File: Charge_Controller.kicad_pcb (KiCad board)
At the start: 2 copper layers, 134.6 x 76.2 mm, 156 parts, among them J1 SOLAR, J10 Conn_01x01_Female, J11 Conn_01x01_Female, J12 Conn_01x01_Female, J13 Conn_01x01_Female, J14 Conn_01x01_Female, J15 Conn_01x01_Female, J16 Conn_01x01_Female, J17 Conn_01x01_Female, J18 Conn_01x01_Female, J19 Conn_01x01_Female, J2 Conn_01x01_Female, J20 Conn_01x01_Female, J21 Conn_01x01_Female, J22 Conn_01x01_Female, J23 Conn_01x01_Female, J24 Conn_01x01_Female, J25 Conn_01x01_Female, J26 Conn_01x01_Female, J27 Conn_01x01_Female, J28 Conn_01x01_Female, J29 Conn_01x01_Female, J3 Conn_01x01_Female, J30 Conn_01x01_Female, J31 Conn_01x01_Female, J32 Conn_01x01_Female, J33 Conn_01x01_Female, J34 Conn_01x01_Female, J36 FAN, J38 I2C_CON, J4 Conn_01x01_Female, J5 Conn_01x01_Female, J6 Conn_01x01_Female, J7 Conn_01x01_Female, J8 BATT, J9 USB_OTG, Q1 CSD19505, Q2 CSD19505, Q3 CSD19505, Q4 Si2306, Q5 2N3904, Q6 2N3904, Q7 PMOS-100V-78A, Q8 PMOS-100V-78A, Q9 Si2306, SW1 RIGHT, SW2 LEFT, SW3 BACK, SW4 SELECT, U1 ACS712-30A, U10 ADS1015, U11 NUP4202, U12 PCF8574, U2 B1212, U3 AMS1117-5.0, U4 AMS1117-3.3, U5 XL7005A, U6 XL7005A, U7 IR2104, U8 ESP32-WROOM-32, U9 CH340C

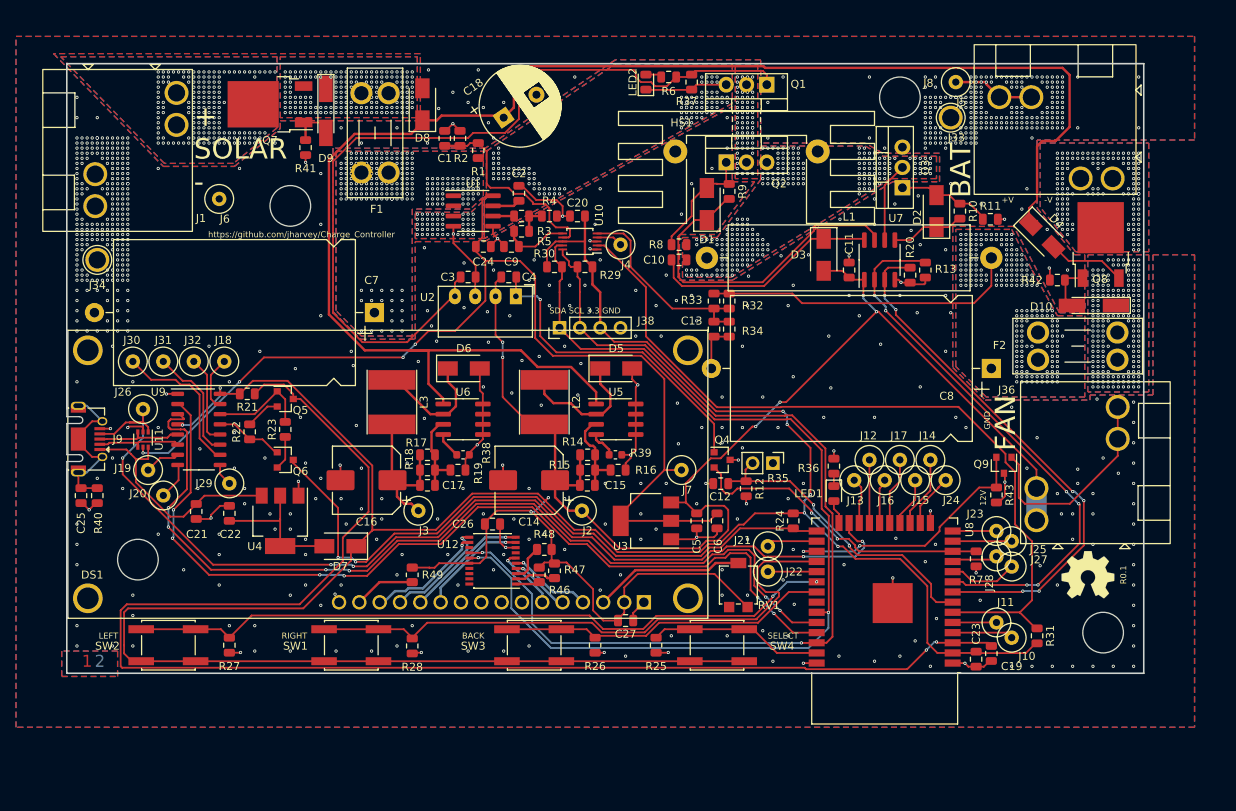
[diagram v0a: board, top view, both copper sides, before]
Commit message: Attempting to export a BOM, save before doing something potentially risky.
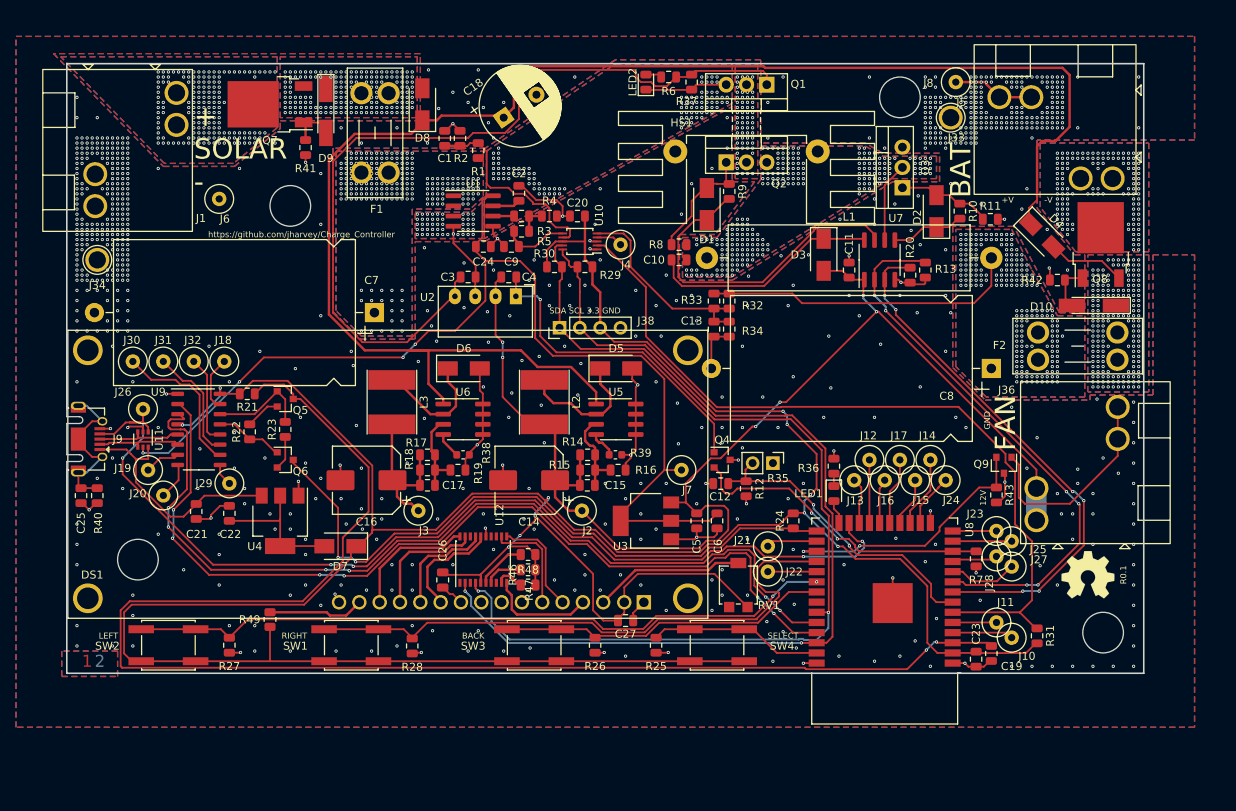
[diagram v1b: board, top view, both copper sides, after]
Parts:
- moved R49 18.6 mm to (91.8, 137.3), turned to 90 degrees
- moved C26 9.35 mm to (113.4, 132.4), turned to 90 degrees
- moved R48 4.89 mm to (124.1, 133.0)
- moved R47 3.30 mm to (124.1, 131.1), turned to 180 degrees
- moved R46 2.90 mm to (124.1, 129.2), turned to 180 degrees
- moved U12 1.15 mm to (118.5, 129.8), turned to 90 degrees
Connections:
- DS1 pad 4: /RW -> /RS
- DS1 pad 5: /RS -> /RW
- U12 pad 1: Net-(R46-Pad2) -> unconnected-(U12-Pad1)
- U12 pad 10: Net-(DS1-Pad12) -> /RS
- U12 pad 11: Net-(DS1-Pad13) -> /RW
- U12 pad 12: Net-(DS1-Pad14) -> /E
- U12 pad 13: unconnected-(U12-Pad13) -> (no net)
- U12 pad 14: /SCL -> unconnected-(U12-Pad14)
- U12 pad 15: /SDA -> GND
- U12 pad 16: +3.3VA -> Net-(DS1-Pad11)
- U12 pad 17: (no net) -> Net-(DS1-Pad12)
- U12 pad 19: (no net) -> Net-(DS1-Pad13)
- U12 pad 2: Net-(R47-Pad2) -> /SCL
- U12 pad 20: (no net) -> Net-(DS1-Pad14)
- U12 pad 3: Net-(R48-Pad2) -> (no net)
- U12 pad 4: /RS -> /SDA
- U12 pad 5: /RW -> +3.3VA
- U12 pad 6: /E -> Net-(R46-Pad2)
- U12 pad 7: unconnected-(U12-Pad7) -> Net-(R47-Pad2)
- U12 pad 8: GND -> (no net)
- U12 pad 9: Net-(DS1-Pad11) -> Net-(R48-Pad2)
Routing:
- net /RS: track 7.61 -> 13.4 mm, vias 1 -> 0
- net +3.3VA: track 394.4 -> 399.4 mm, vias 9 -> 11
- net /E: track 8.27 -> 12.8 mm, vias 1 -> 0
- net Net-(DS1-Pad15): track 7.65 -> 12.0 mm
- net Net-(R46-Pad2): track 3.04 -> 6.26 mm
- net /SDA: track 127.6 -> 124.7 mm
- net /RW: track 10.5 -> 13.1 mm, vias 1 -> 0
- net /SCL: track 124.6 -> 122.7 mm
- net Net-(DS1-Pad12): track 15.3 -> 13.5 mm, vias 1 -> 0
- net Net-(DS1-Pad14): track 14.7 -> 15.9 mm, vias 1 -> 0
- net Net-(DS1-Pad13): track 13.8 -> 15.0 mm, vias 1 -> 0
- net Net-(R48-Pad2): track 4.75 -> 3.59 mm
- net /S+B+1A: track 191.3 -> 190.5 mm
- net GND: track 132.3 -> 131.9 mm, vias 779 -> 789
- net Net-(DS1-Pad11): track 13.6 -> 13.7 mm, vias 1 -> 0
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
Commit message: Potentially going to release this as the first spin.
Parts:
- U12: footprint Package_SO:SSOP-20_4.4x6.5mm_P0.65mm -> Package_SO:SSOP-20_5.3x7.2mm_P0.65mm
- moved Q2 2.54 mm to (151.4, 80.2)
- moved Q3 2.54 mm to (170.9, 80.8)
- moved Q1 2.54 mm to (151.4, 70.5)
- moved Q8 1.12 mm to (195.7, 91.6)
- moved Q7 1.02 mm to (92.9, 72.9)
- moved U12 0.64 mm to (118.5, 129.2), turned to 0 degrees
- turned RV1 to 0 degrees
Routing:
- net Net-(DS1-Pad14): track 15.9 -> 17.2 mm
- net /RW: track 13.1 -> 14.4 mm
- net GND: track 131.9 -> 130.9 mm, vias 789 -> 788
- net +3.3VA: track 399.4 -> 398.5 mm
- net Net-(DS1-Pad11): track 13.7 -> 14.6 mm
- net Net-(DS1-Pad12): track 13.5 -> 14.4 mm
- net /E: track 12.8 -> 13.7 mm
- net Net-(R48-Pad2): track 3.59 -> 4.20 mm
- net Net-(DS1-Pad13): track 15.0 -> 15.5 mm

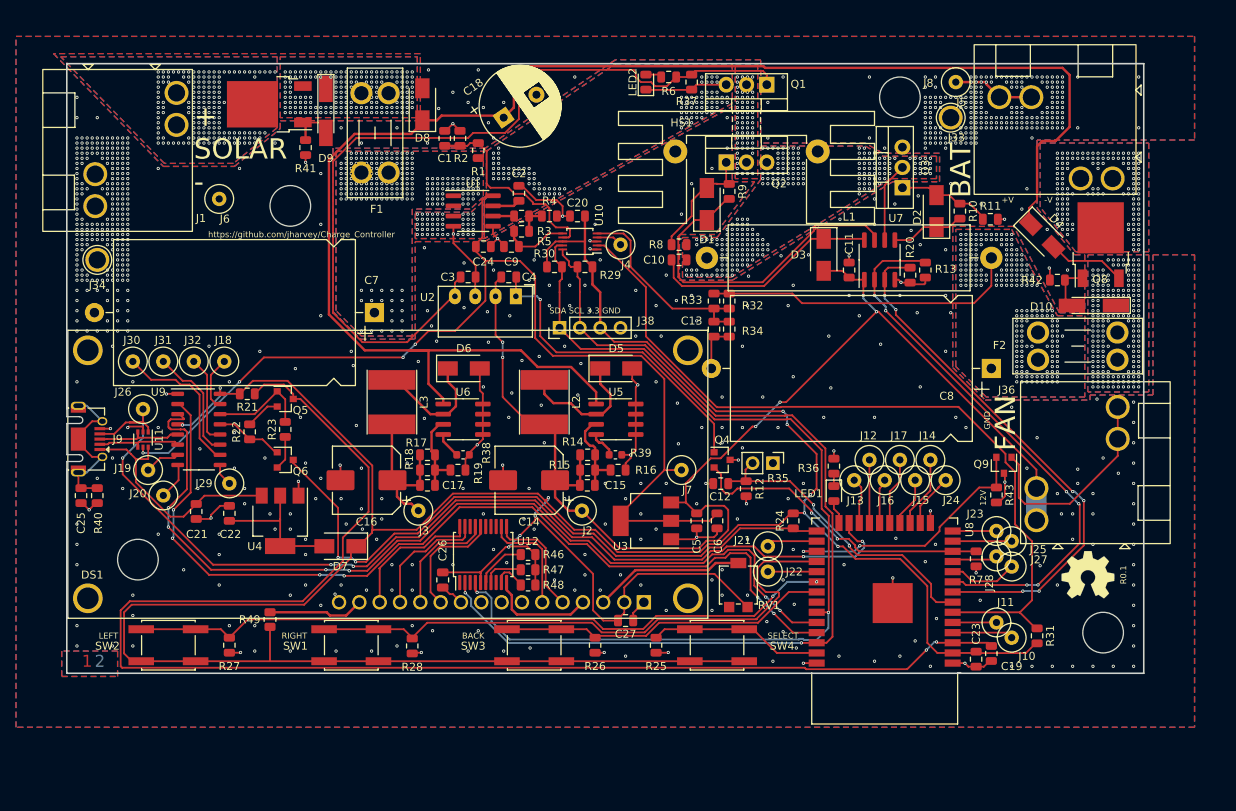
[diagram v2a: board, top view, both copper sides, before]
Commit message: Moved C7 to other side of current sensor, changed C7 and C8 from Axial to Radial, moved U3 slightly. https://github.com/jharvey/Charge_Controller/issues/2
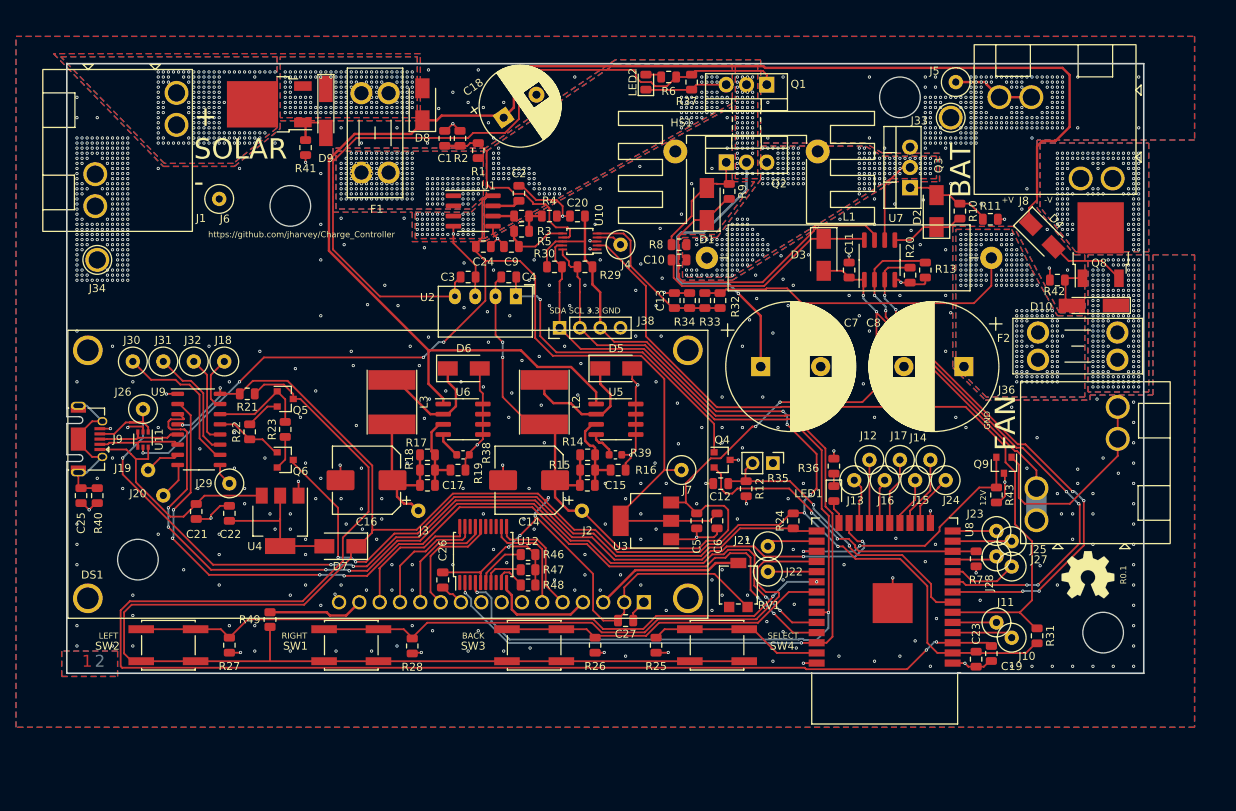
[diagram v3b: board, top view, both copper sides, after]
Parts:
- C7, C8: footprint Capacitor_THT:CP_Axial_L30.0mm_D18.0mm_P35.00mm_Horizontal -> Capacitor_THT:CP_Radial_D16.0mm_P7.50mm
- moved C7 48.8 mm to (153.2, 105.7), turned to 0 degrees
- moved C13 6.11 mm to (142.4, 97.5), turned to 90 degrees
- moved R34 6.11 mm to (144.3, 97.5), turned to 90 degrees
- moved C8 3.44 mm to (178.6, 105.7)
- moved R32 1.14 mm to (148.1, 97.5)
- moved R33 1.14 mm to (146.2, 97.5)
- moved Q3 0.96 mm to (171.9, 80.8)
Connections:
- C7 pad 1: /S+Fused -> /S+Fused3
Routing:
- net /S+Fused3: track 0.00 -> 38.5 mm, vias 63 -> 64
- net Net-(C3-Pad1): track 106.3 -> 97.3 mm
- net /S+B+1A: track 190.5 -> 183.5 mm
- net /12V: track 155.8 -> 161.5 mm
- net /A1: track 25.9 -> 21.1 mm
- net GND: track 130.9 -> 128.0 mm, vias 788 -> 784
- net /B+Fused: track 39.6 -> 41.2 mm
- net Net-(D2-Pad2): track 11.9 -> 10.9 mm
- net /GPIO34: track 98.7 -> 99.4 mm
- net /GPIO32: track 67.0 -> 67.5 mm
- net /S+Fused: vias 196 -> 177
- net /BuckFB: vias 220 -> 225

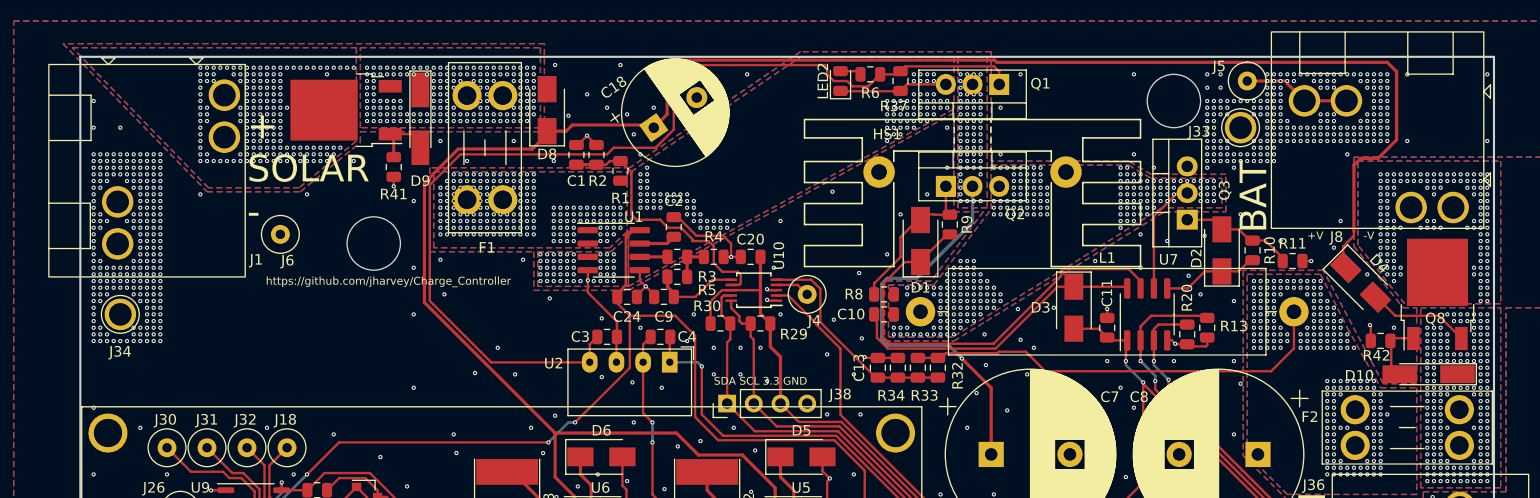
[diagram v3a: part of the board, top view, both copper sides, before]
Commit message: Added D11, D12 and D13 for input surge protection. https://github.com/jharvey/Charge_Controller/issues/3
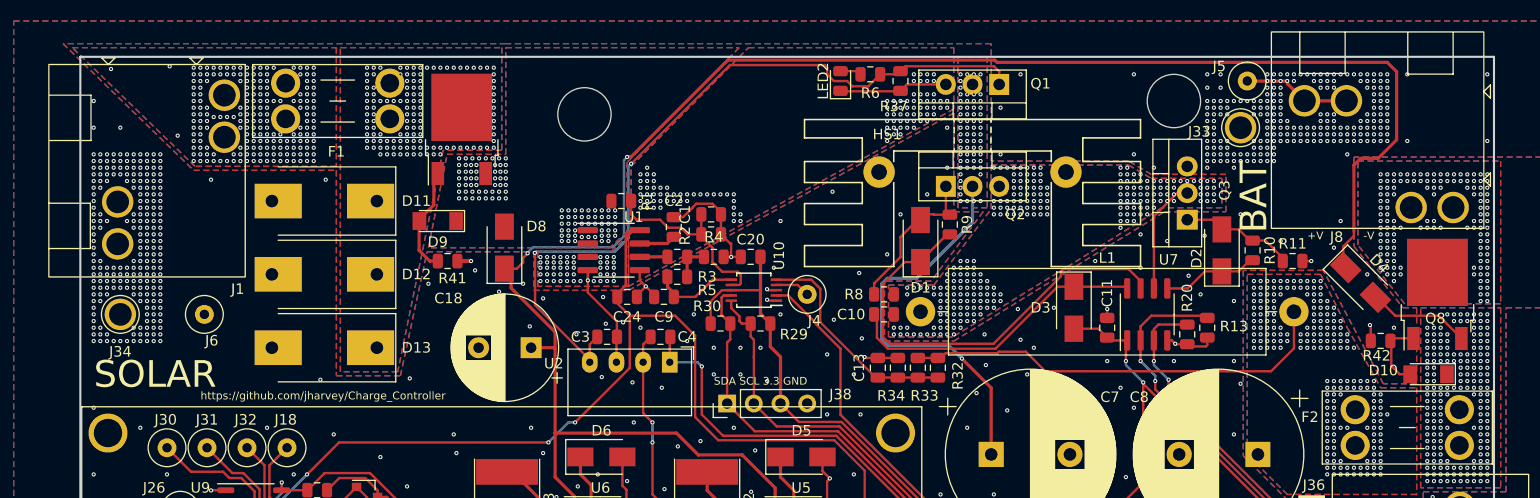
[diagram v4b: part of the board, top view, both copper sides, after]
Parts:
- added D11: 90V-34A, Diode_SMD:D_SMC-RM10_Universal_Handsoldering, F.Cu at (89.7, 81.6)
- added D12: 120V-26A, Diode_SMD:D_SMC-RM10_Universal_Handsoldering, F.Cu at (89.7, 88.6)
- added D13: 120V-26A, Diode_SMD:D_SMC-RM10_Universal_Handsoldering, F.Cu at (89.7, 95.6)
- D10, D9: footprint Diode_SMD:D_MiniMELF_Handsoldering -> Diode_SMD:D_MiniMELF
- moved C18 24.0 mm to (109.4, 95.6), turned to 180 degrees
- moved F1 20.5 mm to (86.0, 70.4), turned to 0 degrees
- moved C1 14.0 mm to (126.5, 82.9), turned to 0 degrees
- moved D8 13.7 mm to (106.8, 86.0)
- moved R2 13.3 mm to (126.5, 84.8), turned to 0 degrees
- moved J6 10.5 mm to (78.3, 92.4)
- moved Q7 10.3 mm to (102.8, 75.9), turned to 90 degrees
- moved R41 10.3 mm to (101.4, 87.3), turned to 0 degrees
- moved D9 9.87 mm to (100.5, 83.5), turned to 180 degrees
- moved R1 2.87 mm to (118.0, 81.6), turned to 0 degrees
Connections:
- F1 pad 1: /S+Fused -> /S+
- F1 pad 2: /S+Polarity -> /S+Fused
- Q7 pad 2: /S+ -> /S+Fused
- R1 pad 1: /S+Fused -> /S+Polarity
- U1 pad 1: /S+Fused -> /S+Polarity
- U1 pad 2: /S+Fused -> /S+Polarity
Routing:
- net Net-(C3-Pad1): track 97.3 -> 75.0 mm, vias 0 -> 2
- net /S+B+1A: track 183.5 -> 172.1 mm, vias 0 -> 2
- net /A3: track 25.5 -> 18.6 mm
- net Net-(D9-Pad2): track 6.36 -> 10.1 mm
- net GND: track 128.0 -> 129.4 mm, vias 784 -> 764
- net Net-(D10-Pad2): track 5.84 -> 6.84 mm
- net /S+Polarity: vias 167 -> 99
- net /S+Fused: vias 177 -> 124
- net /S+: vias 169 -> 196
- net /B+Polarity: vias 173 -> 182
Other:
- outline, holes or cut-outs redrawn
- board text added: "SOLAR"
- board text removed: "+ SOLAR -"
